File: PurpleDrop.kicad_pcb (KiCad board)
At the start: 4 copper layers, 161 x 92 mm, 145 parts, among them J1 Conn_02x32_Odd_Even, J10 current shunt, J2 Conn_02x32_Odd_Even, J3 Conn_02x20_Odd_Even, J4 Conn_01x04, J5 Conn_01x04, J6 Conn_01x04, J7 Conn_02x04_Odd_Even, J8 Conn_02x10_Odd_Even, J9 Barrel_Jack_Switch, Q1 SSM3K329R, Q2 SSM3K329R, Q3 SSM3K329R, Q4 SSM3K329R, SW1 SW_SPDT, U1 HV507, U10 TL7702B, U11 LR8N8-G, U2 HV507, U3 74LVC2T45DCT, U4 74LVC2T45DCT, U5 74LVC2T45DCT, U6 MAX31865AA, U7 MAX31865AA, U8 PCA9685PW, U9 MAX31865AA

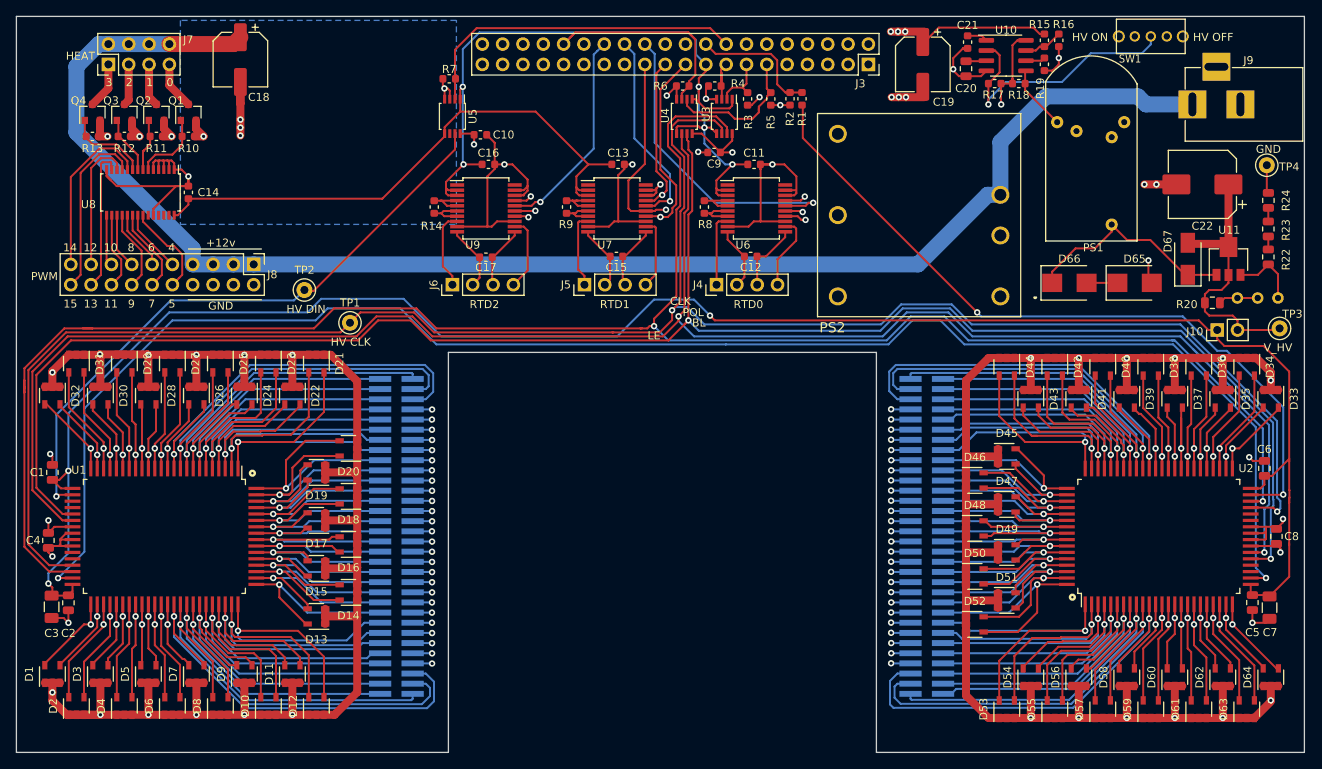
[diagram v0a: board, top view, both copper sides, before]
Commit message: fixed lost mounting holes and artwork from last rev
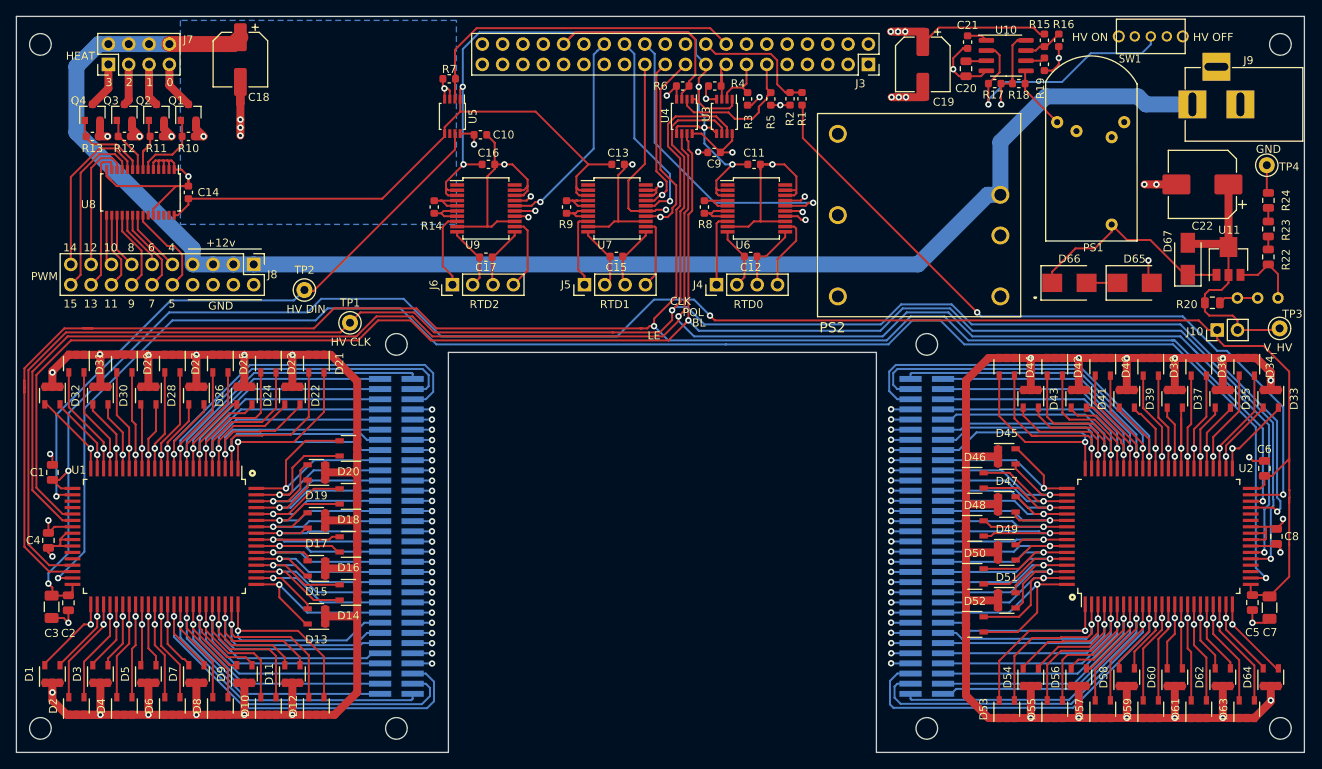
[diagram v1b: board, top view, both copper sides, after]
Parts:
- added G1: W logo, logos:wlogo, B.Cu at (114.3, 50.8)
- added G2: MISL logo, logos:misl-logo, B.Cu at (108.0, 55.9)
- added G3: PurpleDrop logo, logos:purpledrop, B.Cu at (110.5, 74.9)
- added H1: MountingHole, MountingHole:MountingHole_2.7mm_M2.5_ISO14580, F.Cu at (75.5, 58.5)
- added H2: MountingHole, MountingHole:MountingHole_2.7mm_M2.5_ISO14580, F.Cu at (75.5, 144.0)
- added H3: MountingHole, MountingHole:MountingHole_2.7mm_M2.5_ISO14580, F.Cu at (230.5, 144.0)
- added H5: MountingHole, MountingHole:MountingHole_2.7mm_M2.5_ISO14580, F.Cu at (120.0, 96.0)
- added H6: MountingHole, MountingHole:MountingHole_2.7mm_M2.5_ISO14580, F.Cu at (186.3, 96.0)
- added H7: MountingHole, MountingHole:MountingHole_2.7mm_M2.5_ISO14580, F.Cu at (230.5, 58.5)
- added H8: MountingHole, MountingHole:MountingHole_2.7mm_M2.5_ISO14580, F.Cu at (186.3, 144.0)
- added He: MountingHole, MountingHole:MountingHole_2.7mm_M2.5_ISO14580, F.Cu at (120.0, 144.0)
- R14, R8, R9: value 4k0 -> 4k02
